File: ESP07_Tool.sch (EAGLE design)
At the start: 38 parts

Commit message: Sync with .brd
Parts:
- removed C8: 47pF, SparkFun-Capacitors:CAP
- removed IO2: (no value), SparkFun-Connectors:M02PTH
- removed JP1: (no value), SparkFun-Connectors:M05PTH
- removed R10, R9: 330, SparkFun-Resistors:RESISTOR0805-RES
- C1, C2: value 10uF -> 1uF
- C5: value 4.7uF -> 0.1uF; device SparkFun-Capacitors:CAP1210 -> SparkFun-Capacitors:CAP
- C6: value 0.1uF -> 47pF
- R5, R6: value 10K -> 330
- RESET: device SparkFun-Connectors:M02PTH -> SparkFun-Resistors:RESISTOR2010
- RUN: device SparkFun-Connectors:M02PTH -> SparkFun-Connectors:M08SILK_FEMALE_PTH
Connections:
- net 3V3: now also R3.2; no longer R3.1, R5.2, R6.1
- net GND: now also RESET.1; no longer C8.2, IO2.2, RESET.2
- net N$10: now also RUN.4; no longer JP1.3, R3.2
- net N$14: now also R5.1; no longer R9.1
- net N$19: now also R6.1; no longer R10.1
- net N$22: now also R3.1, RESET.2; no longer R5.1, RESET.1
- net N$23: now also C6.1; no longer C8.1
- net N$3: now also RUN.6; no longer JP1.5
- net N$7: now also RUN.3; no longer IO2.1, JP1.2, R6.2
- net N$8: no longer JP1.1
- net N$9: now also RUN.5; no longer JP1.4
- net RXD: now also RUN.7
- net TXD: now also RUN.8
- net VCC: now also R5.2, R6.2; no longer C6.1, R10.2, R9.2
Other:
- moved on the sheet: C5, C6, FLASH, R3, R5, R6

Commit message: Update ESP07_Tool.sch
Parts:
- added R10, R9: 10K, SparkFun-Resistors:RESISTOR0805-RES
- renumbered RUN to JP1
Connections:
- removed net N$16: JP2.4, U$1.P$12
- new net N$1: JP2.3, U$1.P$12
- net 3V3: now also JP2.6
- net GND: now also R10.1
- net N$11: no longer JP2.2
- net N$15: now also JP2.2, R9.1; no longer JP2.3
- net N$17: now also JP2.4; no longer JP2.5
- net N$18: now also JP2.5; no longer JP2.6
- net N$22: now also R9.2
- net N$8: now also R10.2
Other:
- moved on the sheet: LED, R8

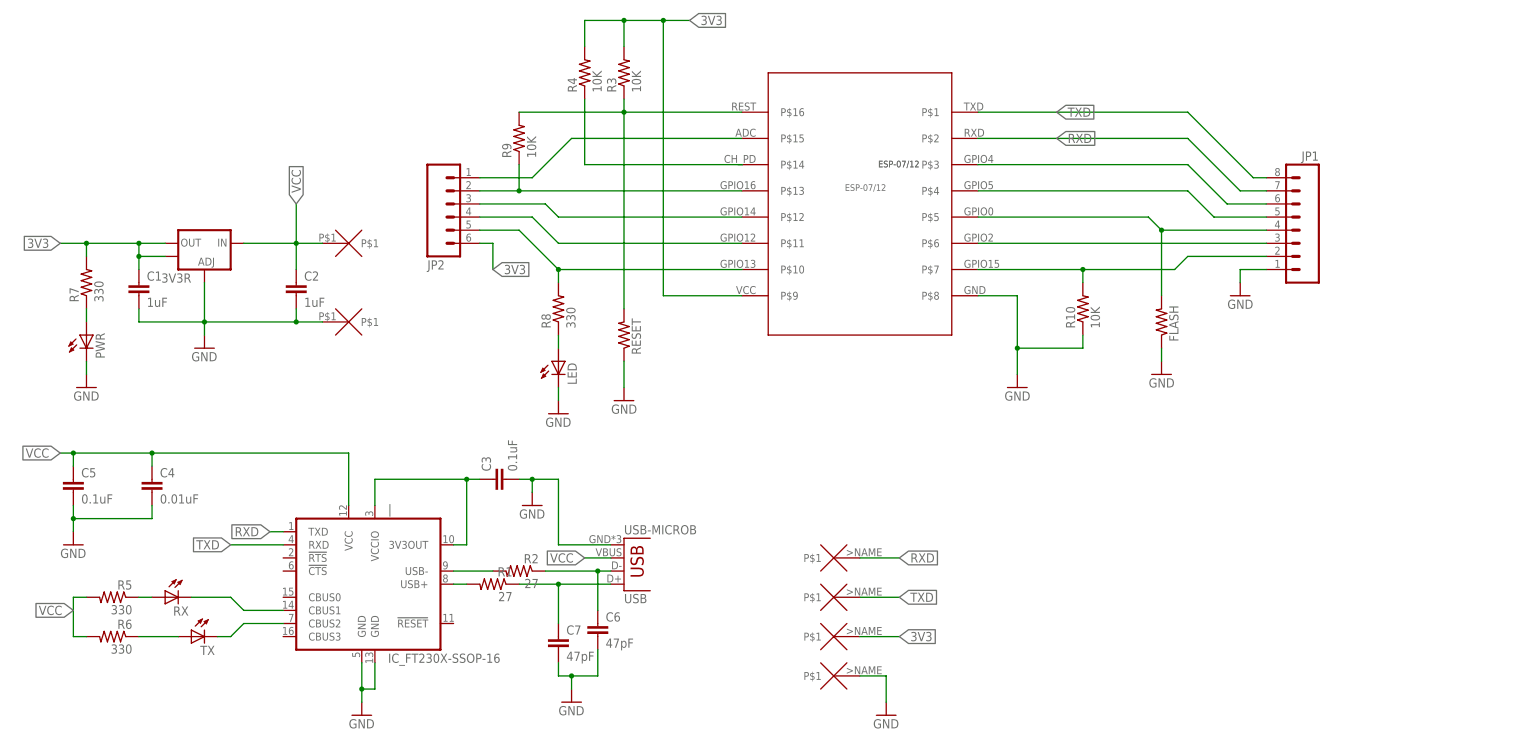
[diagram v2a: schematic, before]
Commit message: Switched to MCP1824ST-3302E/DB
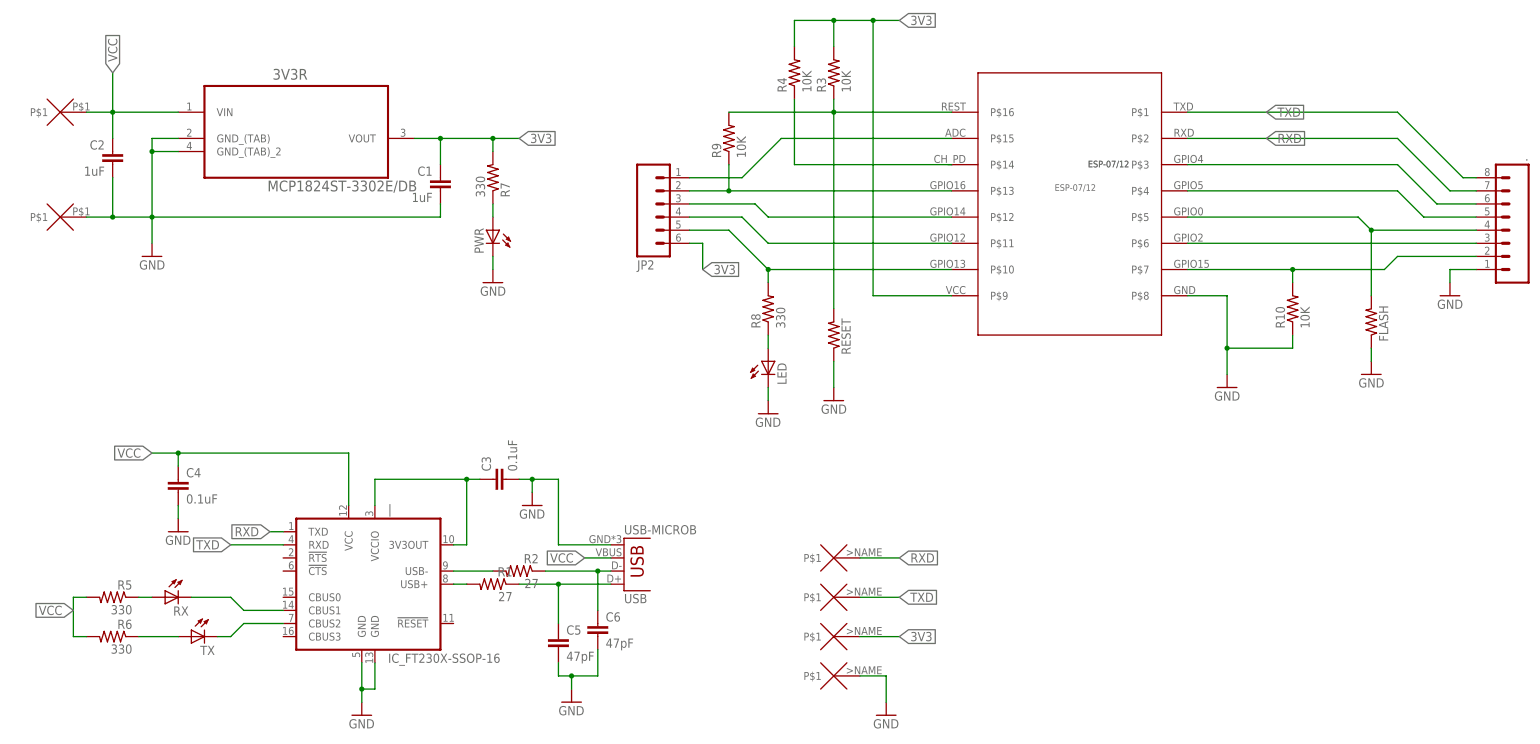
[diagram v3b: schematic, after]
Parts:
- removed C7: 47pF, SparkFun-Capacitors:CAP
- removed JP1: (no value), SparkFun-Connectors:M08SILK_FEMALE_PTH
- added .: (no value), SparkFun-Connectors:M08SILK_FEMALE_PTH
- 3V3R: value (none) -> MCP1824ST-3302E/DB; device SparkFun-PowerIC:V_REG_LM1117SOT223 -> Microchip_By_element14_Batch_1:MCP1824ST-3302E/DB
- C4: value 0.01uF -> 0.1uF
- C5: value 0.1uF -> 47pF
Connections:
- net 3V3: now also 3V3R.VOUT; no longer 3V3R.OUT, 3V3R.OUT@1
- net GND: now also ..1, 3V3R.GND_(TAB), 3V3R.GND_(TAB)_2; no longer 3V3R.ADJ, C7.2, JP1.1
- net N$10: now also ..4; no longer JP1.4
- net N$26: now also C5.1; no longer C7.1
- net N$3: now also ..6; no longer JP1.6
- net N$7: now also ..3; no longer JP1.3
- net N$8: now also ..2; no longer JP1.2
- net N$9: now also ..5; no longer JP1.5
- net RXD: now also ..7; no longer JP1.7
- net TXD: now also ..8; no longer JP1.8
- net VCC: now also 3V3R.VIN; no longer 3V3R.IN, C5.1
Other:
- moved on the sheet: C1, C2, C4, C5, FLASH, JP2, LED, PWR, R10, R3, R4, R7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
